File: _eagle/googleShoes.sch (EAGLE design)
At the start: 37 parts, among them U1 MCP73831, U2 3.3V, U3 ATMEGA328, Y1 8MHz

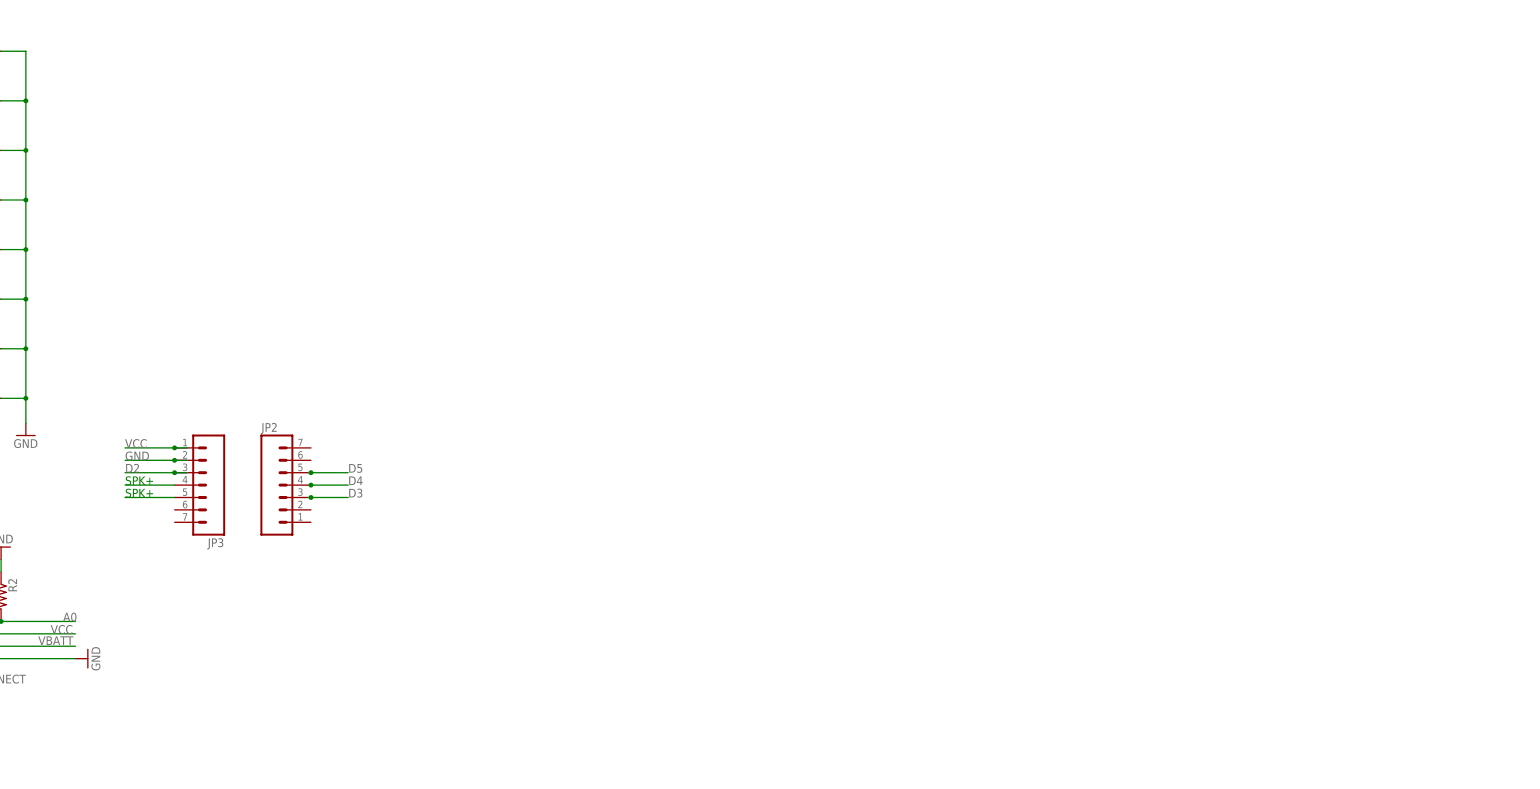
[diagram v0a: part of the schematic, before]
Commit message: added amplifier. needs routing.
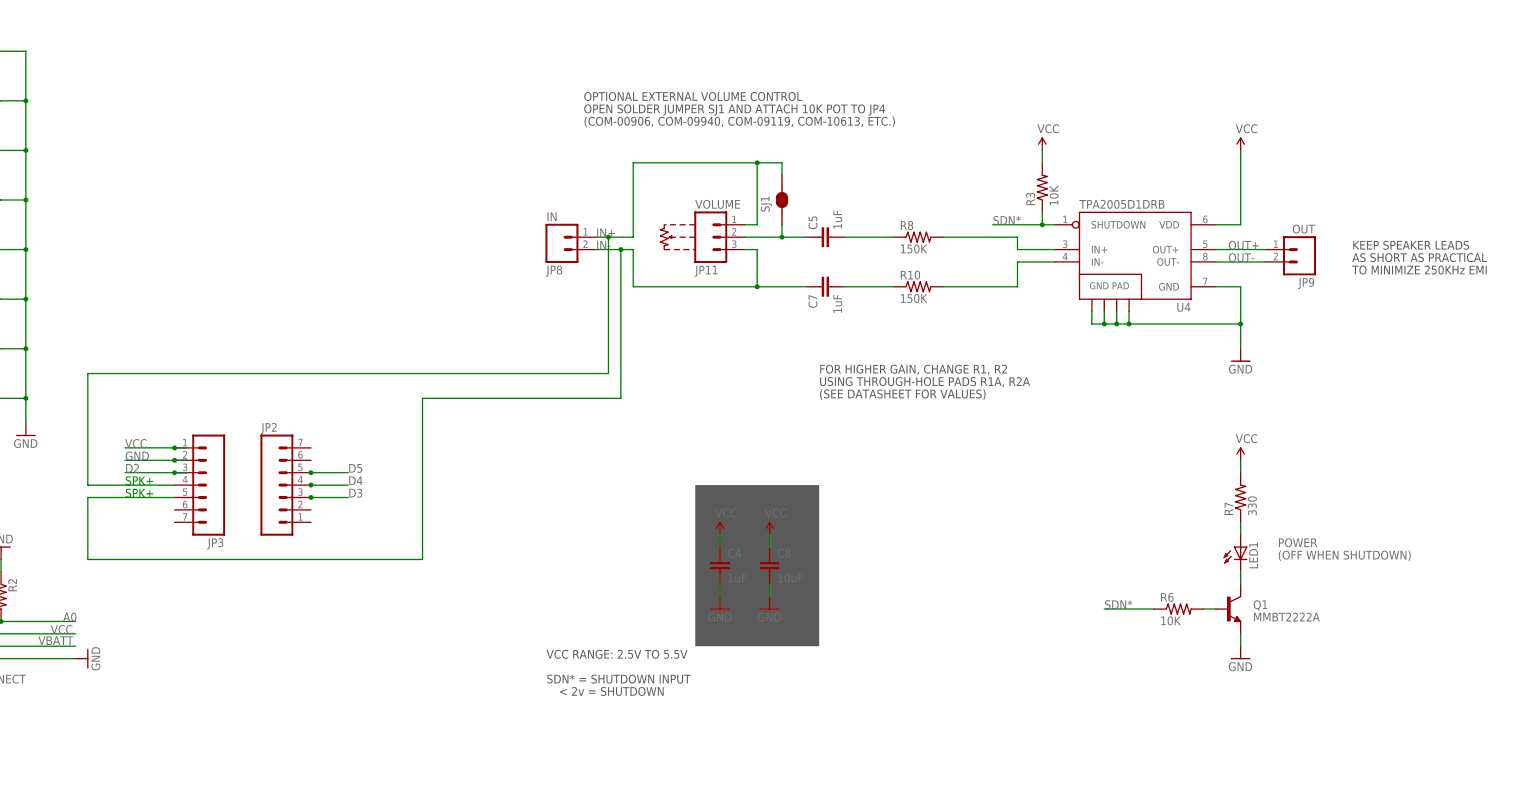
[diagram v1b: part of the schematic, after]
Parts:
- added C4, C5, C7: 1uF, SparkFun:CAP1206
- added C8: 10uF, SparkFun:CAP1206
- added JP11: VOLUME, SparkFun:M03PTH
- added JP8: IN, SparkFun:M02PTH
- added JP9: OUT, SparkFun:M02PTH
- added LED1: (no value), led:LEDCHIPLED_0805
- added Q1: MMBT2222A, SparkFun:TRANSISTOR_NPNSOT23-3
- added R10, R8: 150K, resistor:R-US_M0805
- added R3, R6: 10K, resistor:R-US_M0805
- added R7: 330, resistor:R-US_M0805
- added SJ1: SOLDERJUMPERNC2, SparkFun:SOLDERJUMPERNC2
- added U4: TPA2005D1DRB, mike-temp:TPA2005D1DRB
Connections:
- removed net SPK+: JP3.4
- removed net SPK-: JP3.5
- new net IN+: JP11.1, JP3.4, JP8.1, SJ1.2
- new net IN+AMP: R8.2, U4.IN+
- new net IN-: C7.1, JP11.3, JP3.5, JP8.2
- new net IN-AMP: R10.2, U4.IN-
- new net N$1: C5.1, JP11.2, SJ1.1
- new net N$18: LED1.A, R7.1
- new net N$19: Q1.B, R6.2
- new net N$20: LED1.C, Q1.C
- new net N$21: C5.2, R8.1
- new net N$22: C7.2, R10.1
- new net OUT+: JP9.1, U4.OUT+
- new net OUT-: JP9.2, U4.OUT-
- new net SDN*: R3.1, R6.1, U4.SHUTDOWN
- net GND: now also C4.2, C8.2, Q1.E, U4.GND@1, U4.GND@2, U4.GND@3, U4.GND@4, U4.GND@5
- net VCC: now also C4.1, C8.1, R3.2, R7.2, U4.VDD
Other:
- note added: "(COM-00906, COM-09940, COM-09119, COM-10613, ETC.)"
- note added: "(OFF WHEN SHUTDOWN)"
- note added: "(SEE DATASHEET FOR VALUES)"
- note added: "< 2v = SHUTDOWN"
- note added: "AS SHORT AS PRACTICAL"
- note added: "FOR HIGHER GAIN, CHANGE R1, R2"
- note added: "KEEP SPEAKER LEADS"
- note added: "OPEN SOLDER JUMPER SJ1 AND ATTACH 10K POT TO JP4"
- note added: "OPTIONAL EXTERNAL VOLUME CONTROL"
- note added: "POWER"
- note added: "SDN* = SHUTDOWN INPUT"
- note added: "TO MINIMIZE 250KHz EMI"
- note added: "USING THROUGH-HOLE PADS R1A, R2A"
- note added: "VCC RANGE: 2.5V TO 5.5V"

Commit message: board layout
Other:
- note added: "there are decouplers in the main circuit, are these still needed?"
- note removed: "< 2v = SHUTDOWN"
- note removed: "SDN* = SHUTDOWN INPUT"
- note removed: "VCC RANGE: 2.5V TO 5.5V"
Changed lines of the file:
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@@
 <text x="332.74" y="101.6" size="1.778" layer="97">USING THROUGH-HOLE PADS R1A, R2A</text>
 <text x="332.74" y="99.06" size="1.778" layer="97">(SEE DATASHEET FOR VALUES)</text>
-<text x="276.86" y="40.64" size="1.778" layer="97">SDN* = SHUTDOWN INPUT</text>
-<text x="279.4" y="38.1" size="1.778" layer="97">&lt; 2v = SHUTDOWN</text>
-<text x="276.86" y="45.72" size="1.778" layer="97">VCC RANGE: 2.5V TO 5.5V</text>
 <text x="284.48" y="154.94" size="1.778" layer="97">(COM-00906, COM-09940, COM-09119, COM-10613, ETC.)</text>
 <text x="441.96" y="129.54" size="1.778" layer="97">KEEP SPEAKER LEADS</text>
@@
 <rectangle x1="324.866" y1="139.192" x2="325.374" y2="140.208" layer="94"/>
 <rectangle x1="307.34" y1="48.26" x2="332.74" y2="81.28" layer="97"/>
+<text x="312.42" y="45.72" size="1.778" layer="97">there are decouplers in the main circuit, are these still needed?</text>
 </plain>
 <instances>
